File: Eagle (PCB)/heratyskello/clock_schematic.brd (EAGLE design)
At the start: 100 x 81 mm, 27 parts, among them IC1 DS3231/SO, J1 USB-B-S

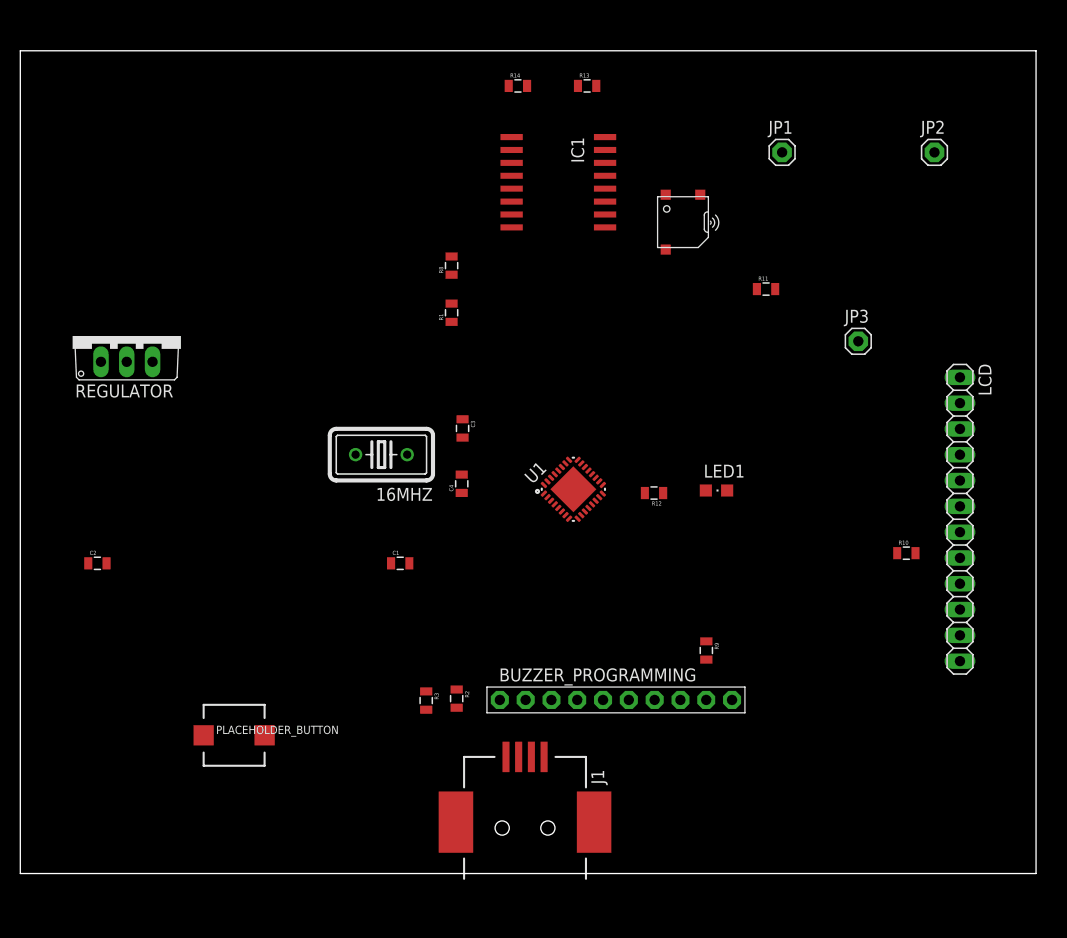
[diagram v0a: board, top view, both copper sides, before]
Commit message: Eagle paths almost made
Most of the paths are made. Only regulator replacement needed.
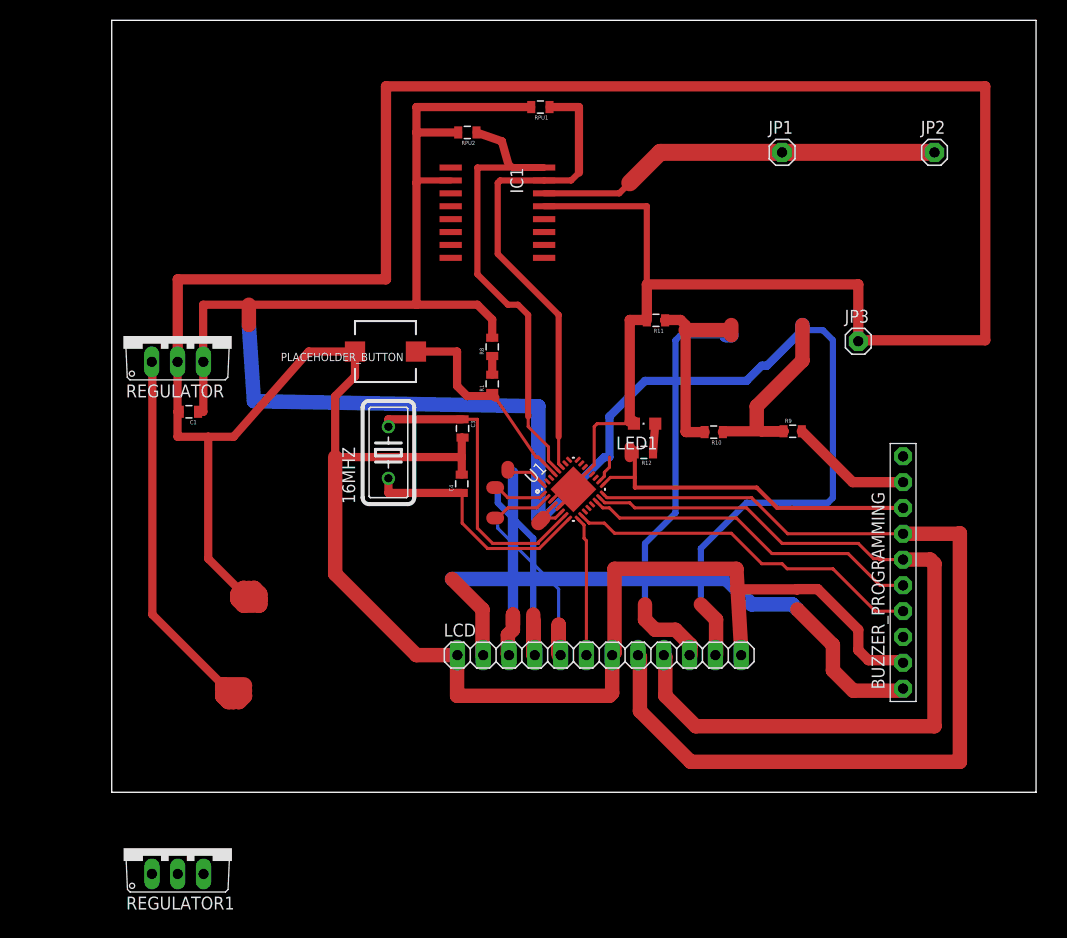
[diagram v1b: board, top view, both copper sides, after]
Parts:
- removed C2: 0.1uF, SparkFun-Capacitors:0805
- removed J1: USB-B-S, SparkFun-Connectors:USB-B-SMT
- removed PLACEHOLDER_BUZZER: SMT-0540-S-R, adafruit:SMT-0540-S-R
- removed R13, R14: (no value), SparkFun-Resistors:0805
- removed R2, R3: 68, SparkFun-Resistors:0805
- added REGULATOR1: 786TV, linear:TO220V
- added RPU1, RPU2: 2250, SparkFun-Resistors:0805
- moved PLACEHOLDER_BUTTON 40.6 mm to (36.0, 50.4), turned to 180 degrees
- moved LCD 37.9 mm to (57.0, 20.5), turned to 0 degrees
- moved BUZZER_PROGRAMMING 30.9 mm to (86.9, 28.6), turned to 90 degrees
- moved C1 25.6 mm to (16.6, 44.5), turned to 180 degrees
- moved R9 23.2 mm to (76.0, 42.5), turned to 0 degrees
- moved R10 22.4 mm to (68.3, 42.5), turned to 180 degrees
- moved R11 11.3 mm to (62.6, 53.5), turned to 180 degrees
- moved LED1 9.67 mm to (61.5, 43.3), turned to 90 degrees
- moved R8 8.94 mm to (46.5, 50.9)
- moved R1 8.06 mm to (46.5, 47.2)
- moved IC1 6.71 mm to (47.0, 64.1)
- moved REGULATOR 5.00 mm to (15.5, 51.9)
- moved R12 4.12 mm to (61.4, 40.5)
- moved 16MHZ 0.72 mm to (36.2, 40.5), turned to 90 degrees
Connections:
- removed net 3V_BATTERY-: JP3.1
- removed net D13: BUZZER_PROGRAMMING.6
- removed net N$23: BUZZER_PROGRAMMING.8
- removed net N$31: C2.1
- removed net N$33: J1.D-, R2.2
- removed net N$34: J1.D+, R3.2
- net 5V: now also LCD.11, RPU1.2, RPU2.2; no longer BUZZER_PROGRAMMING.1, J1.VUSB, LCD.5
- net A0: no longer LCD.1
- net A1: no longer LCD.2
- net A2: no longer LCD.3
- net A3: no longer LCD.4
- net A4: now also RPU1.1
- net A5: now also RPU2.1
- net D10: now also BUZZER_PROGRAMMING.5; no longer BUZZER_PROGRAMMING.3
- net D11: now also BUZZER_PROGRAMMING.6; no longer BUZZER_PROGRAMMING.4
- net D12: now also BUZZER_PROGRAMMING.7, LCD.8; no longer BUZZER_PROGRAMMING.5, LCD.10
- net D2: now also LCD.3; no longer R3.1
- net D3: now also LCD.4
- net D4: now also LCD.5; no longer R2.1
- net D5: now also LCD.6; no longer PLACEHOLDER_BUZZER.-
- net D6: now also BUZZER_PROGRAMMING.4
- net GND: now also JP3.1, LCD.1; no longer J1.GND, LCD.11, PLACEHOLDER_BUZZER.+
- net LCD_V0: now also LCD.10; no longer LCD.8
- net LED_D13: now also BUZZER_PROGRAMMING.8
- net LIGHT_SWITCH-: now also BUZZER_PROGRAMMING.1, LCD.2; no longer BUZZER_PROGRAMMING.10, LCD.6
- net RESET: no longer C2.2
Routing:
- net GND: track 0.00 -> 407.4 mm
- net 5V: track 0.00 -> 239.0 mm
- net D12: track 0.00 -> 98.5 mm
- net D11: track 0.00 -> 83.5 mm
- net LCD_V0: track 0.00 -> 62.5 mm
- net LIGHT_SWITCH-: track 0.00 -> 59.3 mm
- net A5: track 0.00 -> 48.9 mm
- net A4: track 0.00 -> 48.4 mm
- net 3V_BATTERY+: track 0.00 -> 40.1 mm
- net VIN: track 0.00 -> 38.9 mm
- net D6: track 0.00 -> 35.6 mm
- net LED_D13: track 0.00 -> 34.2 mm
- net D10: track 0.00 -> 33.7 mm
- net N$1: track 0.00 -> 30.7 mm
- net N$2: track 0.00 -> 24.5 mm
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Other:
- board size 100 x 81 mm -> 91 x 76 mm

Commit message: Eagle File Complete
Regulator was moved to make the PCB smaller. Also moved the 5V connection that was under the 3V battery case lower so it wouldn't be left under the battery.
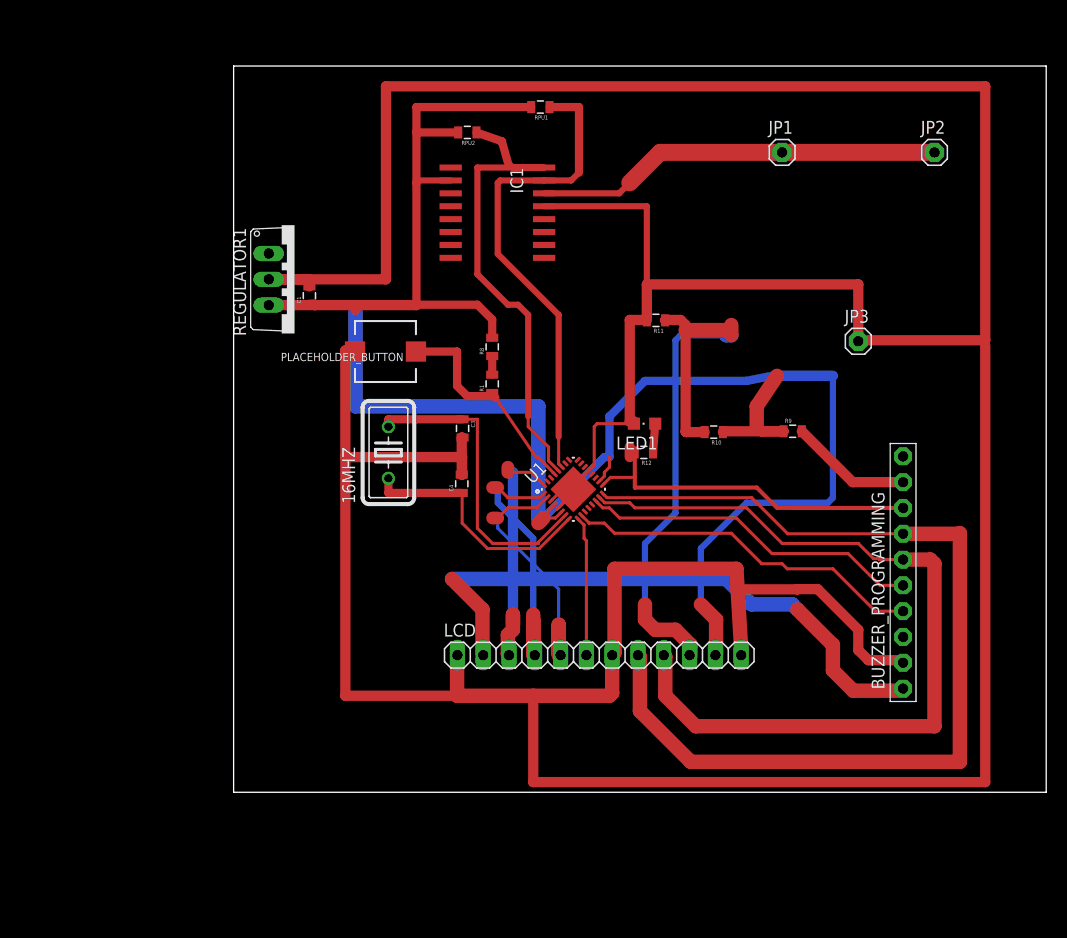
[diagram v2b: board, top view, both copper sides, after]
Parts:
- removed REGULATOR: 786TV, linear:TO220V
- moved REGULATOR1 57.2 mm to (27.0, 57.5), turned to 270 degrees
- moved C1 16.5 mm to (28.5, 55.9), turned to 90 degrees
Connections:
- net 5V: now also REGULATOR1.3; no longer REGULATOR.3
- net GND: now also REGULATOR1.2; no longer REGULATOR.2
- net VIN: now also REGULATOR1.1; no longer REGULATOR.1
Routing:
- net VIN: track 38.9 -> 0.00 mm
- net 5V: track 239.0 -> 200.2 mm
- net GND: track 407.4 -> 442.8 mm
- net N$6: track 6.12 -> 0.00 mm
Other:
- board size 91 x 76 mm -> 80 x 71.5 mm

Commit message: Eagle Ground fill done. Ready to print.
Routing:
- net N$6: track 0.00 -> 11.5 mm
- net GND: track 442.8 -> 449.3 mm
- added copper zone on layer 1, net GND

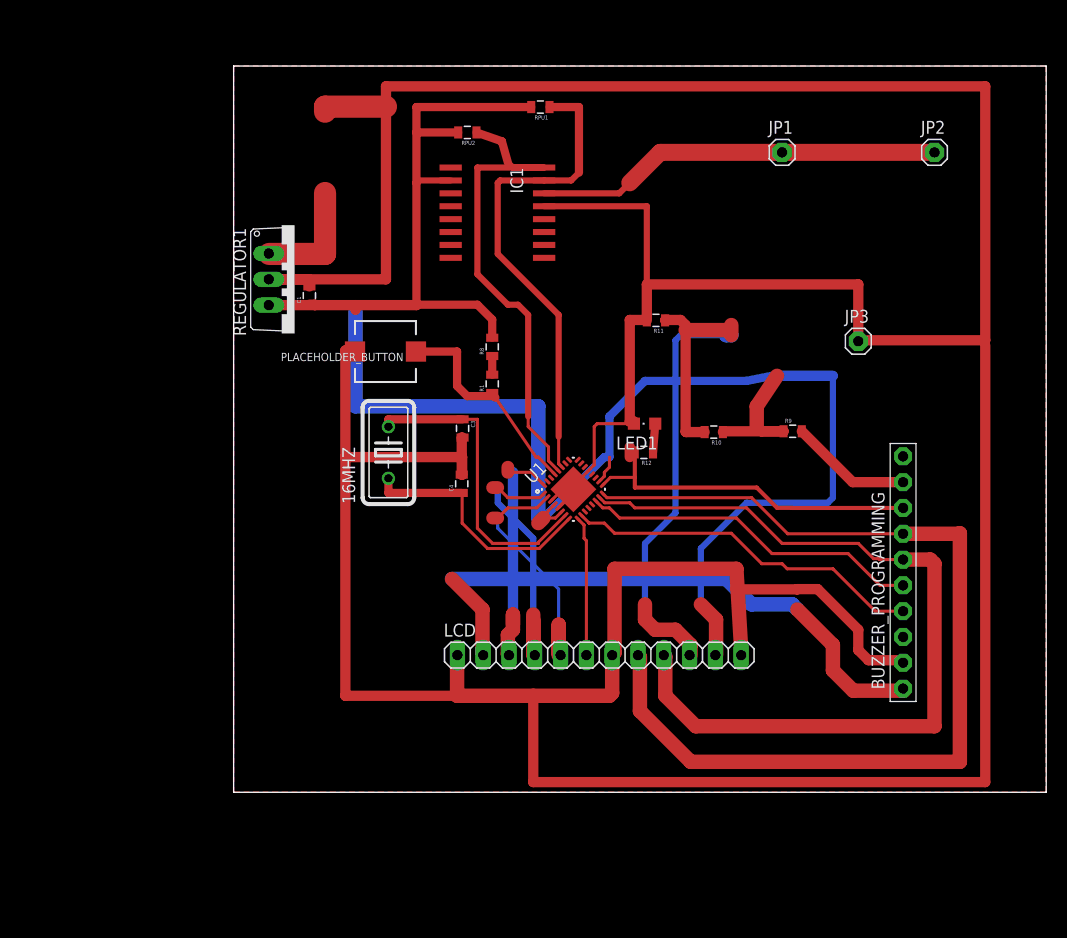
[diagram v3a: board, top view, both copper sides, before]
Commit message: Eagle Fuckup Corrected
Atmega is now the correct size.
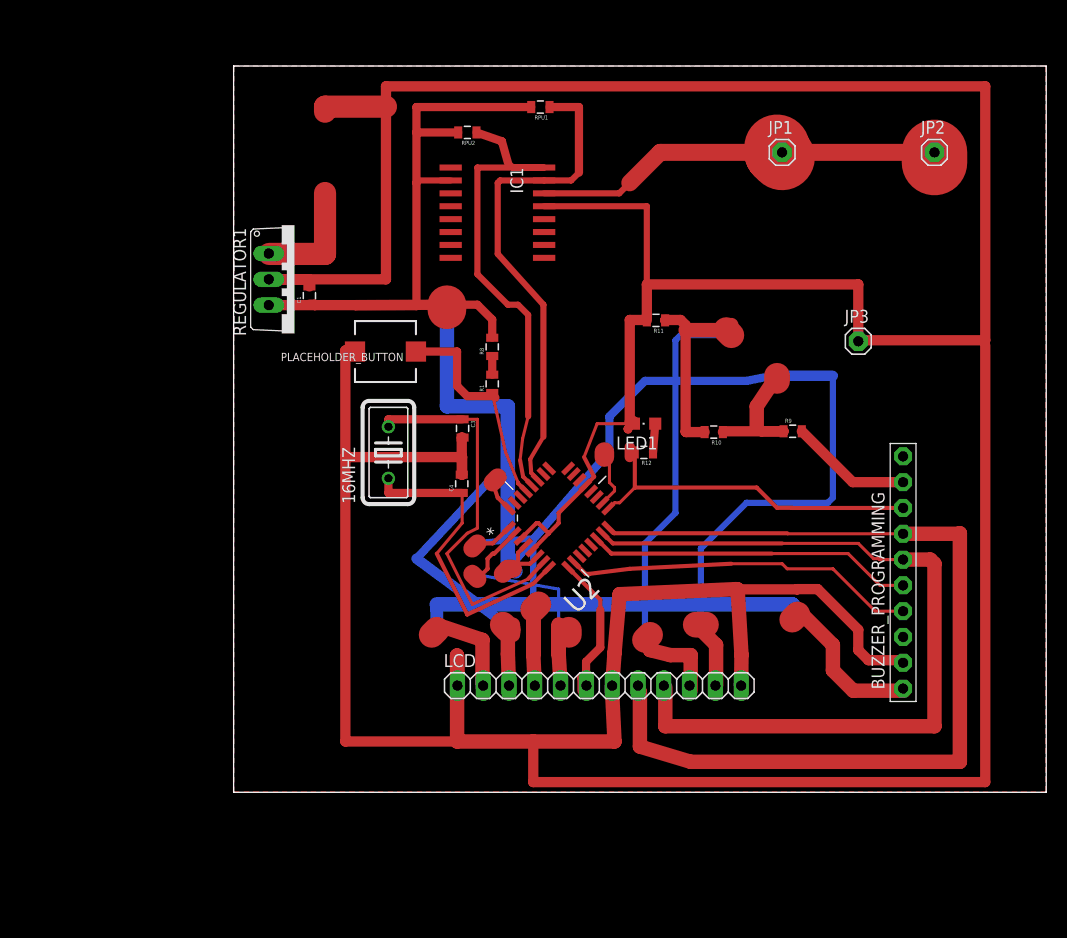
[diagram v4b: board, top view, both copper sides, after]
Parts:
- removed U1: (no value), SparkFun-DigitalIC:MLF32-PAD
- added U2: ATMEGA328P-AU, Atmel_By_element14_Batch_1-00:QFP80P900X900X120-32N
- moved LCD 3.00 mm to (57.0, 17.5)
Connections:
- removed net N$1: 16MHZ.2, C3.1, U1.7
- removed net N$2: 16MHZ.1, C4.1, U1.8
- new net CRYSTAL1: 16MHZ.2, C3.1, U2.7
- new net CRYSTAL2: 16MHZ.1, C4.1, U2.8
- net 5V: now also U2.18, U2.4, U2.6; no longer U1.18, U1.4, U1.6
- net A0: now also U2.23; no longer U1.23
- net A1: now also U2.24; no longer U1.24
- net A2: now also U2.25; no longer U1.25
- net A3: now also U2.26; no longer U1.26
- net A4: now also U2.27; no longer U1.27
- net A5: now also U2.28; no longer U1.28
- net A6: now also U2.19; no longer U1.19
- net A7: now also U2.22; no longer U1.22
- net AREF: now also U2.20; no longer U1.20
- net D0: now also U2.30; no longer U1.30
- net D1: now also U2.31; no longer U1.31
- net D10: now also U2.14; no longer U1.14
- net D11: now also U2.15; no longer U1.15
- net D12: now also U2.16; no longer U1.16
- net D2: now also U2.32; no longer U1.32
- net D3: now also U2.1; no longer U1.1
- net D4: now also U2.2; no longer U1.2
- net D5: now also U2.9; no longer U1.9
- net D6: now also U2.10; no longer U1.10
- net D7: now also U2.11; no longer U1.11
- net D8: now also U2.12; no longer U1.12
- net D9: now also U2.13; no longer U1.13
- net GND: now also U2.21, U2.3, U2.5; no longer U1.21, U1.3, U1.5, U1.PAD
- net LED_D13: now also U2.17; no longer U1.17
- net RESET: now also U2.29; no longer U1.29
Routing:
- net CRYSTAL1: track 0.00 -> 38.0 mm
- net CRYSTAL2: track 0.00 -> 31.7 mm
- net N$1: track 30.7 -> 0.00 mm
- net N$2: track 24.5 -> 1.00 mm
- net 5V: track 200.2 -> 218.4 mm
- net GND: track 449.3 -> 464.8 mm
- net LCD_V0: track 62.5 -> 71.7 mm
- net D2: track 24.3 -> 32.8 mm
- net D5: track 13.8 -> 18.0 mm
- net D4: track 22.3 -> 25.8 mm
- net D12: track 98.5 -> 95.1 mm
- net D11: track 83.5 -> 80.5 mm
- net LIGHT_SWITCH-: track 59.3 -> 62.3 mm
- net D3: track 23.6 -> 26.5 mm
- net D10: track 33.7 -> 32.0 mm
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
